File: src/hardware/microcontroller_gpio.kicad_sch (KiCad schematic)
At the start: 3 parts

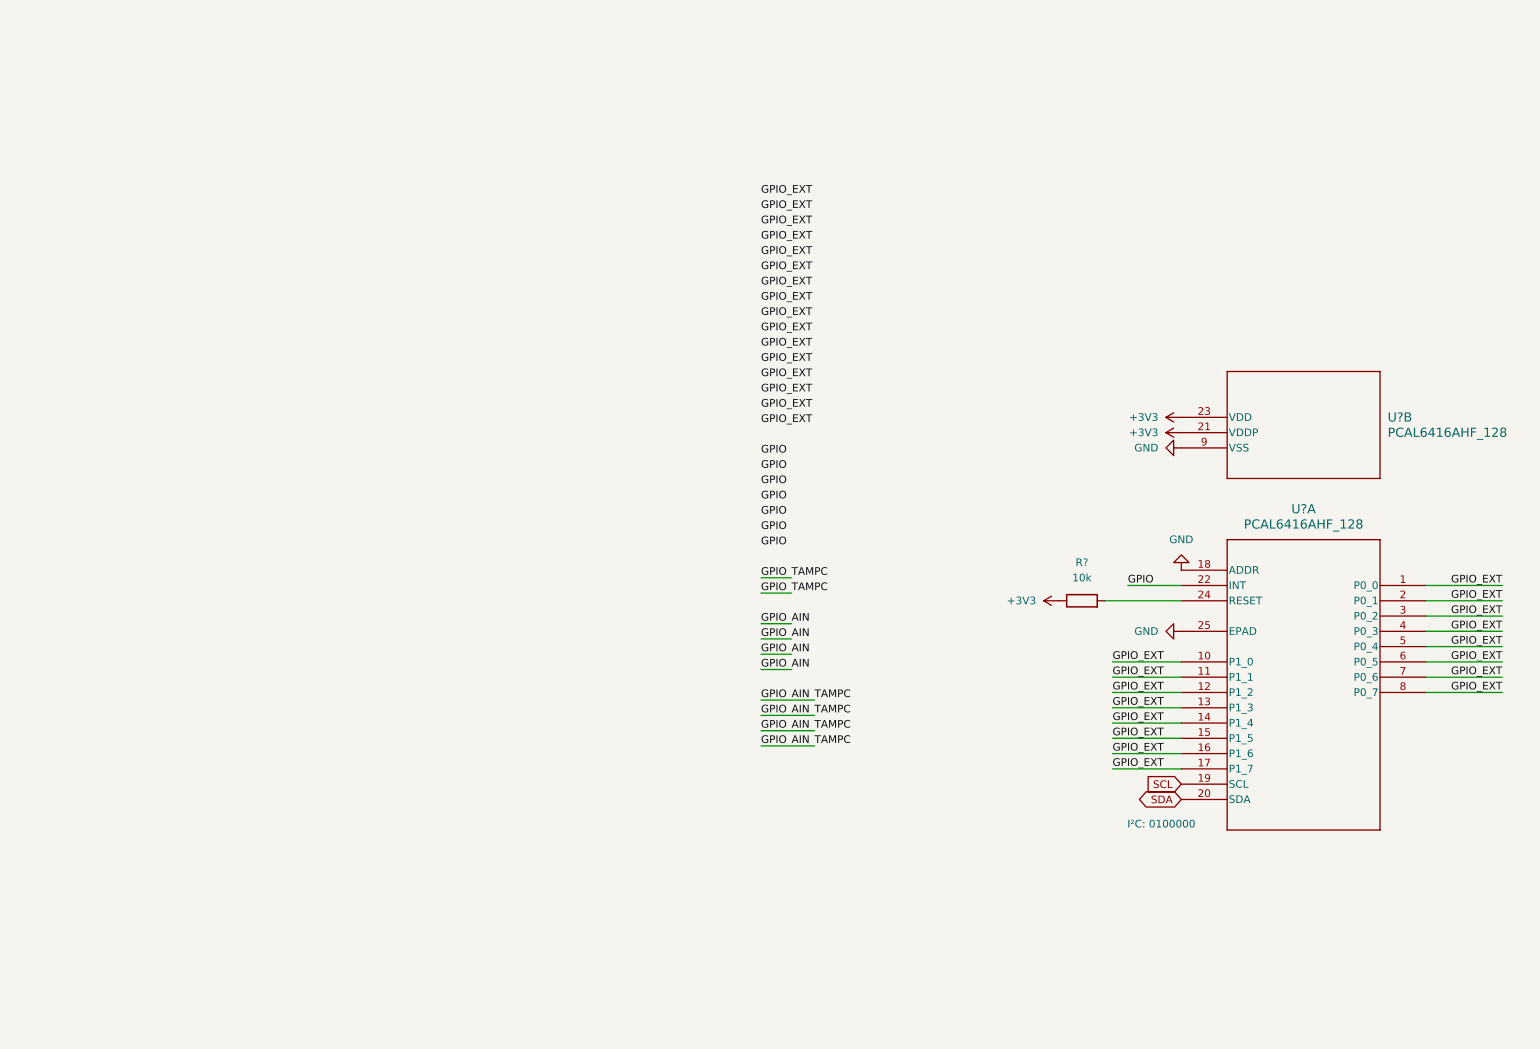
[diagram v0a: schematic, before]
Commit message: Added another GPIO Expander
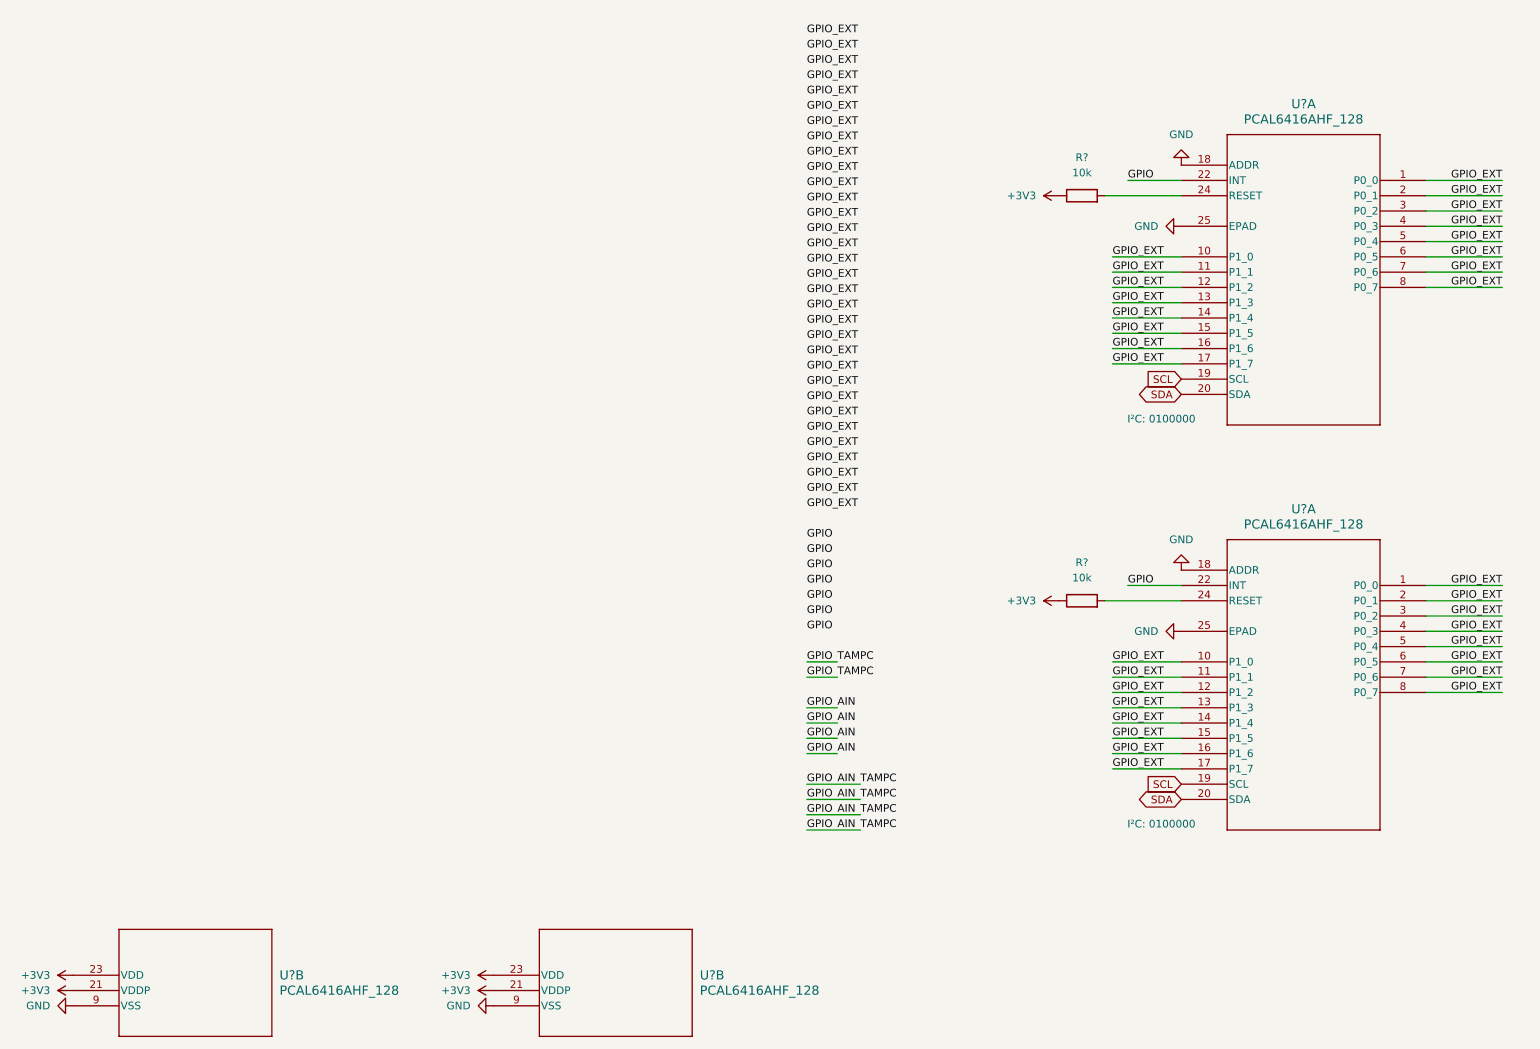
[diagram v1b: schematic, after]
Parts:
- added R?: 10k, symbol Device:R
- added U? (x2): PCAL6416AHF_128, HWQFN24_PCAL_NXP, symbol 2026-10-21_14-05-48:PCAL6416AHF_128
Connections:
- net +3V3: now also R?.1, U?.21 (VDDP), U?.23 (VDD)
- net AIN: now also U?.22 (INT)
- net GND: now also U?.18 (ADDR), U?.25 (EPAD), U?.9 (VSS)
- net GPIO_EXT: now also U?.1 (P0_0), U?.10 (P1_0), U?.11 (P1_1), U?.12 (P1_2), U?.13 (P1_3), U?.14 (P1_4), U?.15 (P1_5), U?.16 (P1_6), U?.17 (P1_7), U?.2 (P0_1), U?.3 (P0_2), U?.4 (P0_3), U?.5 (P0_4), U?.6 (P0_5), U?.7 (P0_6), U?.8 (P0_7)
- net SCL: now also U?.19 (SCL)
- net SDA: now also U?.20 (SDA)
- new net: R?.2, U?.24 (RESET)
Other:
- moved on the sheet: U?B

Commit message: Created Buttons
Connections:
- net +3V3: now also U?.18 (ADDR)
- net GND: no longer U?.18 (ADDR)
- net GPIO_EXT renamed BTN1
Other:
- note added: "I²C: 0100001"

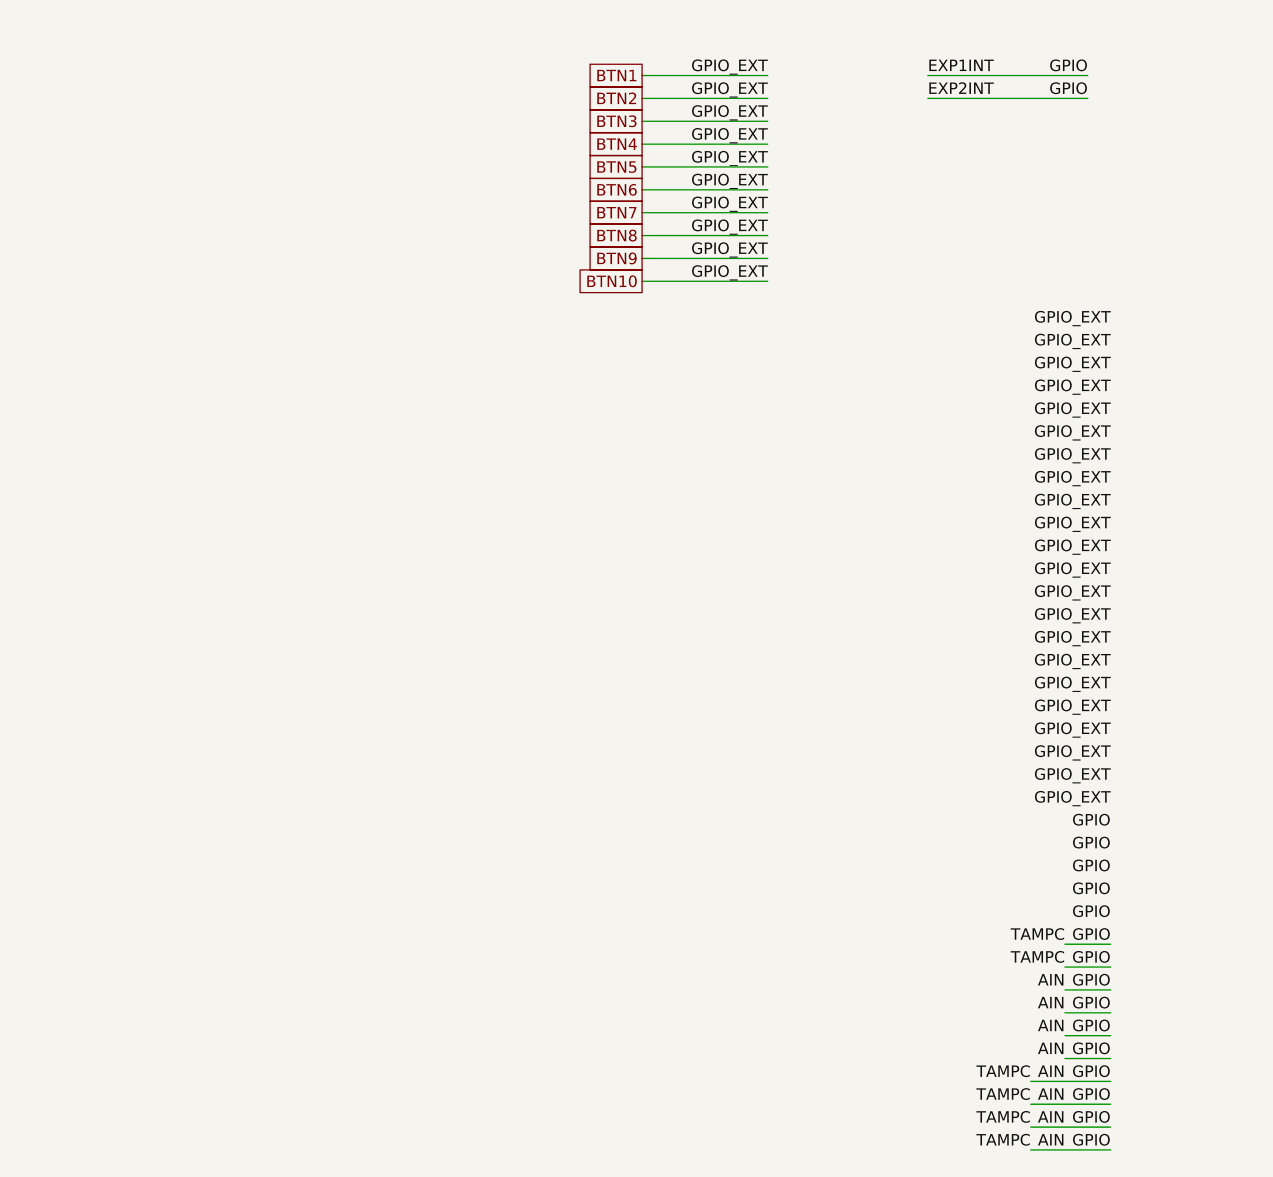
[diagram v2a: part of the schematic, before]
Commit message: Added environment light sensors
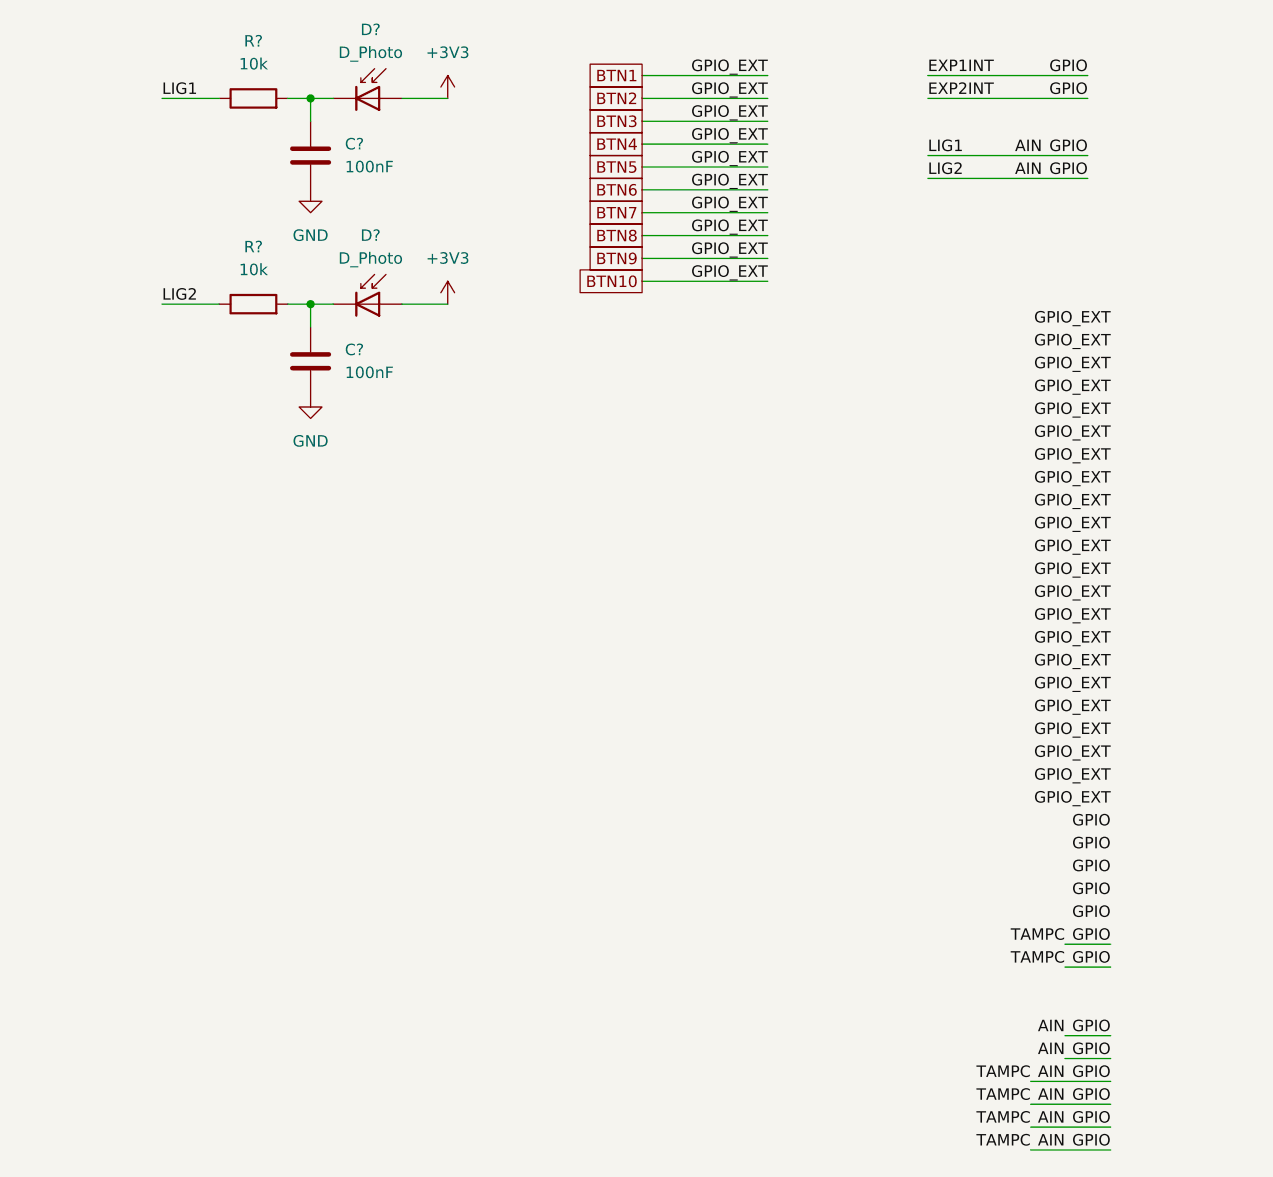
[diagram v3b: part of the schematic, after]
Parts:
- added C? (x2): 100nF, symbol Device:C
- added D? (x2): D_Photo, symbol Device:D_Photo
- added R? (x2): 10k, symbol Device:R
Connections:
- net +3V3: now also D?.2 (A), D?.2 (A)
- net AIN: now also R?.1, R?.1
- net GND: now also C?.2, C?.2
- new net: C?.1, D?.1 (K), R?.2 (x2)
